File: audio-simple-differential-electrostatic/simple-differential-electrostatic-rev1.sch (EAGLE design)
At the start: 73 parts, among them IC1 LT1115, IC2 LT1115, IC3 LT1115, IC4 LT1115, IC5 LM7815, IC7 LM317T, IC8 LM317T, IC9 LM7915, J1 ROUT, J2 LOUT, J3 VIN_PLATE, X1 RIN, X2 LIN, X3 VIN_OPAMP, X4 VIN_HEATER

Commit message: First gerber export
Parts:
- added C26, C30, C31, C32: 10n, rcl:C-EU050-025X075
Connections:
- net GND: now also C26.2, C30.2, C31.2, C32.2; no longer H1.MOUNT, H2.MOUNT, H3.MOUNT, H4.MOUNT
- net PP_HEATER_N: now also C31.1, C32.1
- net PP_HEATER_P: now also C26.1, C30.1
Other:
- note added: "Heater Decoupling"
- note added: "Net Class: high_voltage"
- moved on the sheet: C1, C2, C3, C4

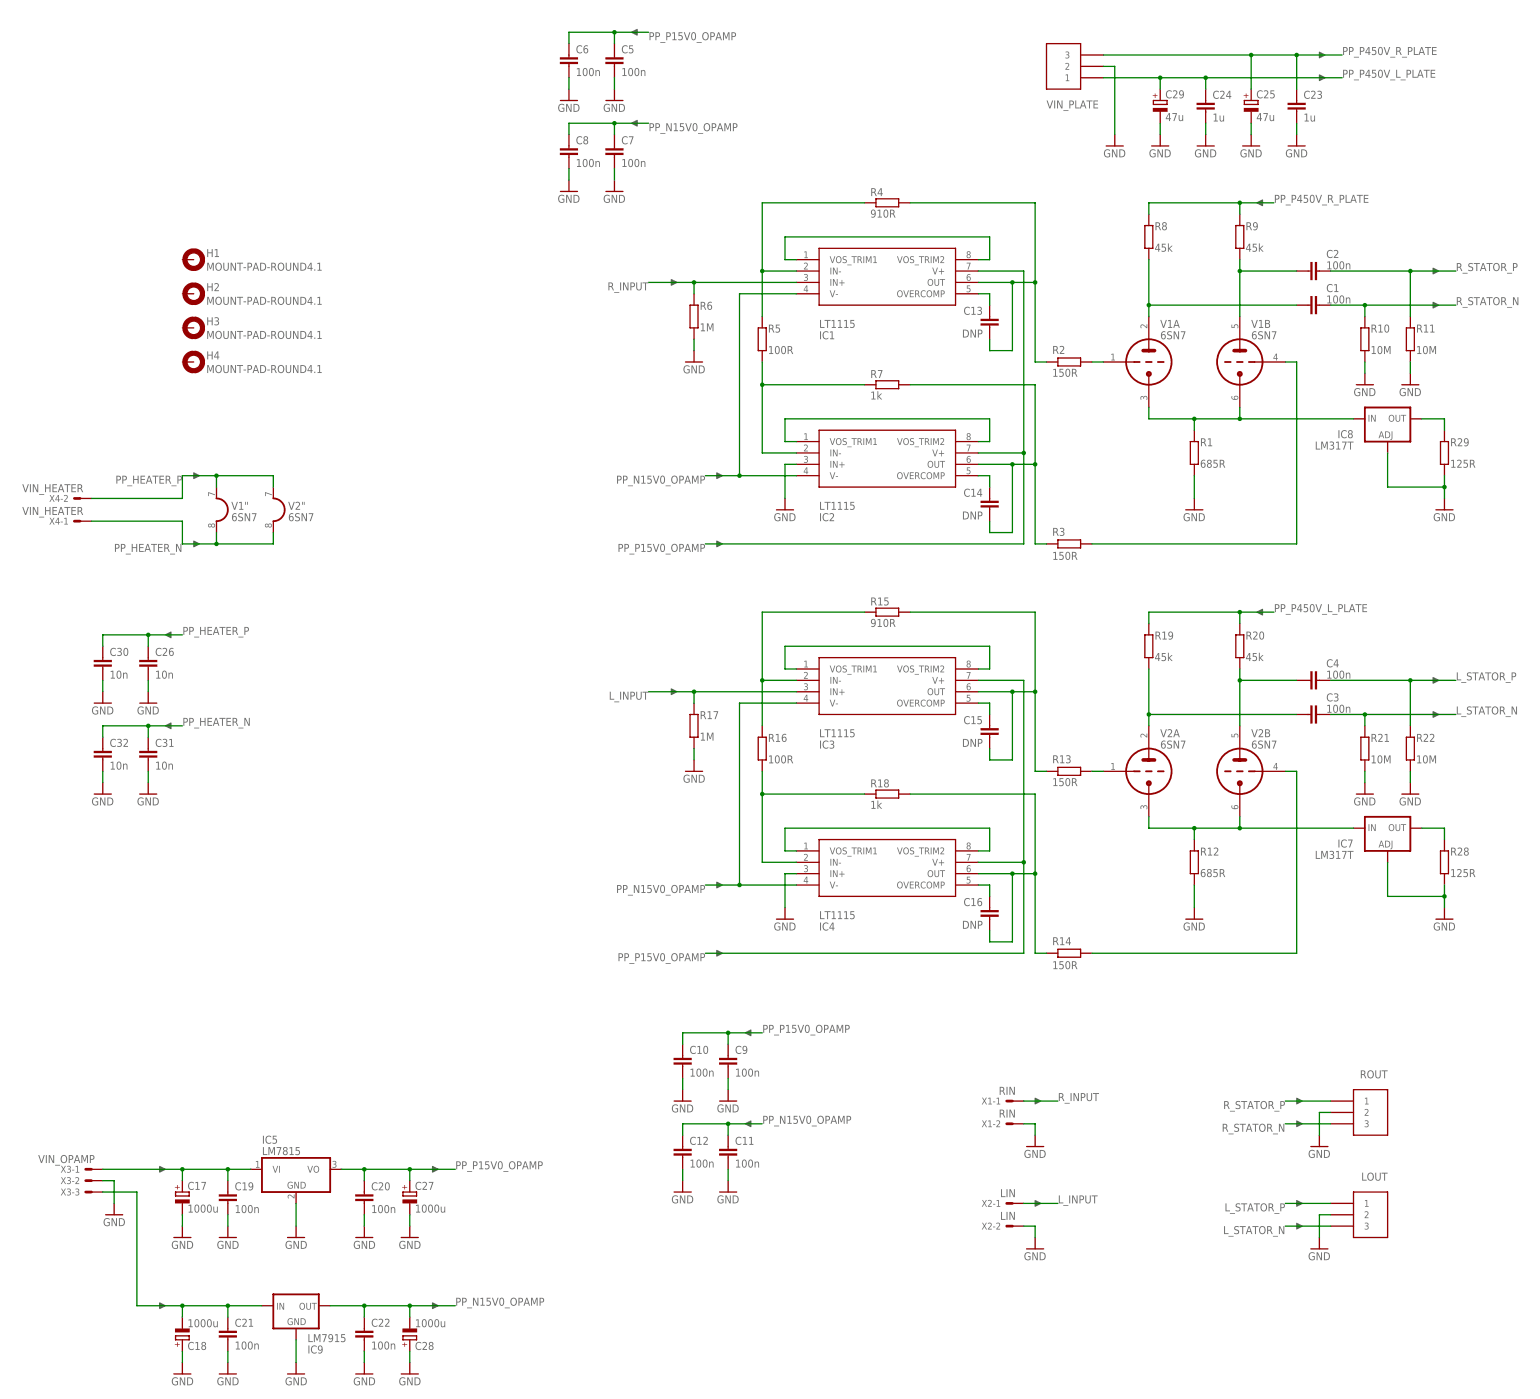
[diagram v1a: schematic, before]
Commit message: Ran cmd-renumber, increased HV clearance to 56mil, re-exported gerbers
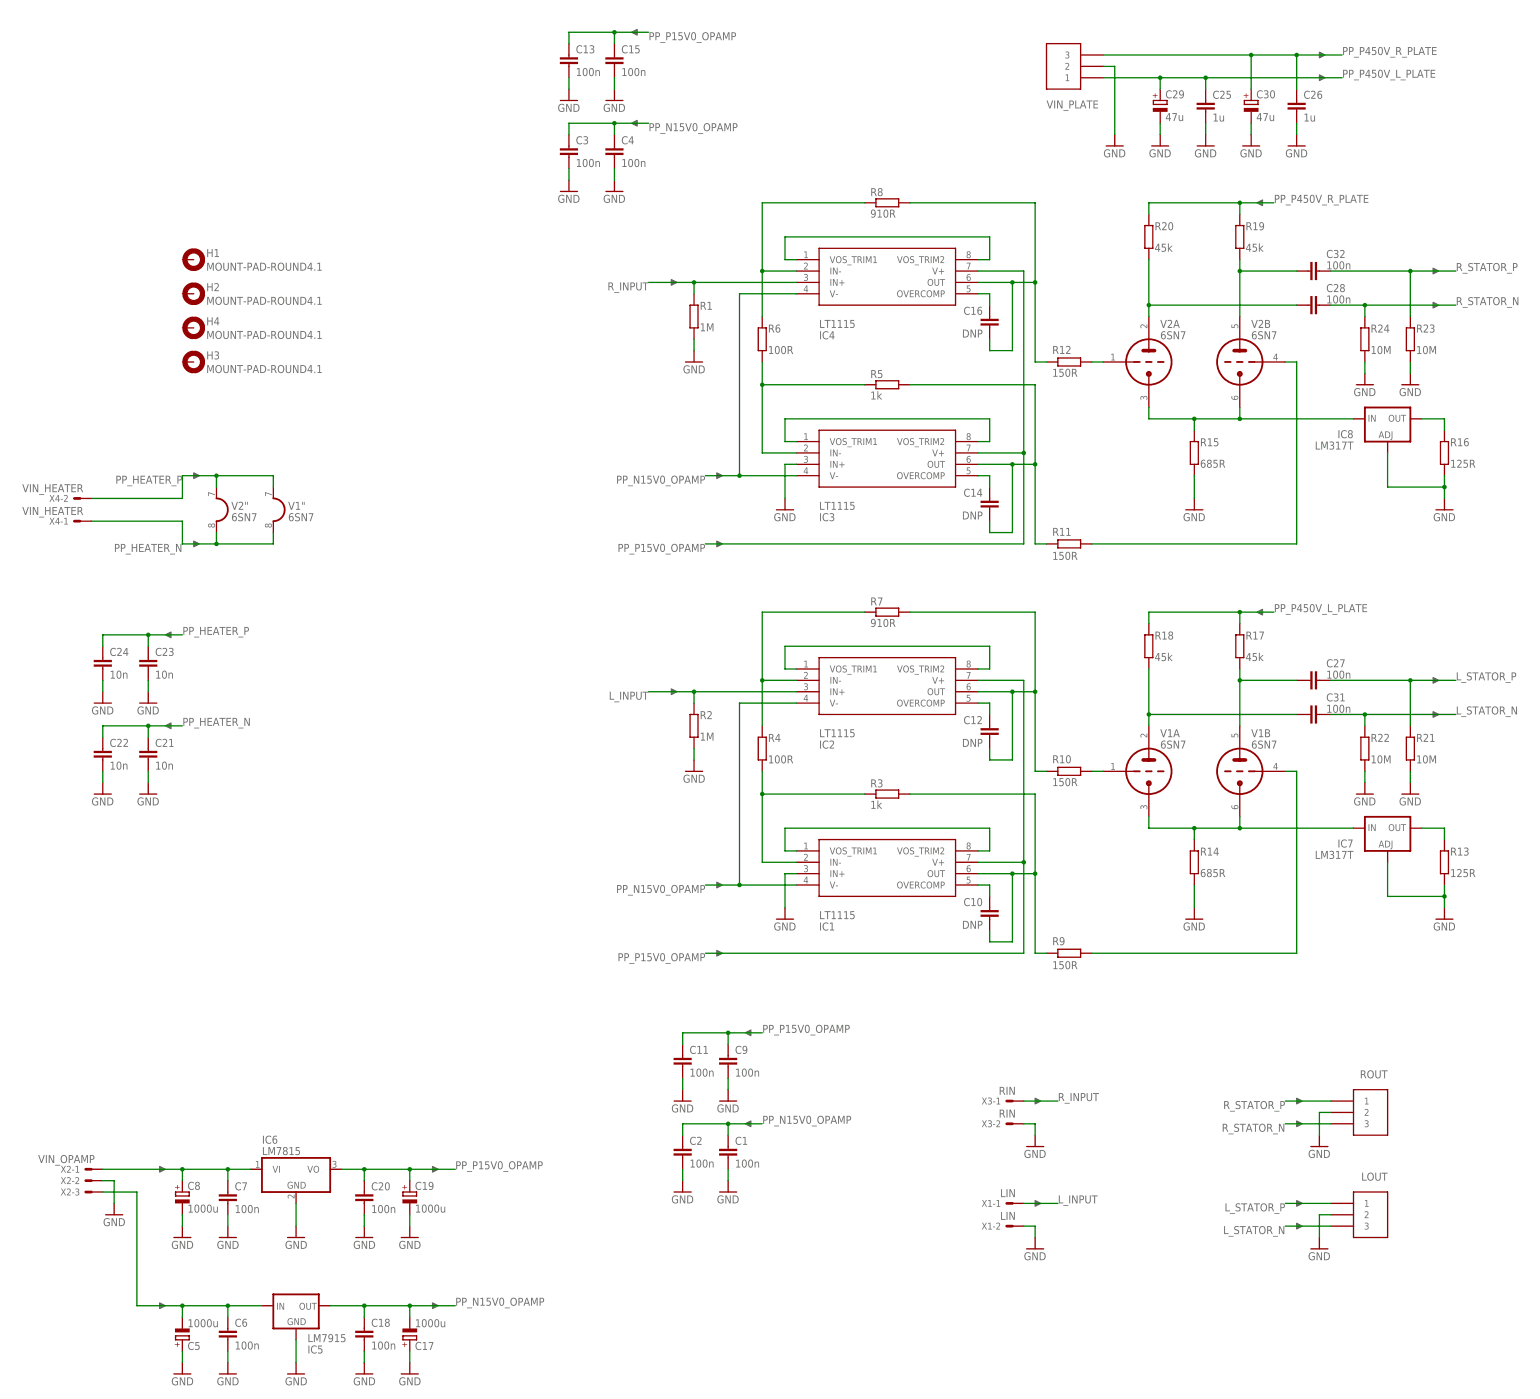
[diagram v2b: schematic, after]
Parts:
- removed IC9: LM7915, v-reg:79XXS
- removed R28, R29: 125R, rcl:R-EU_0309/10
- added IC6: LM7815, linear:7815TV
- added R23, R24: 10M, rcl:R-EU_0309/10
- C1, C2, C3, C4: device rcl:C-EU375-155X418 -> rcl:C-EU050-025X075
- C10, C12: value 100n -> DNP
- C13, C15: value DNP -> 100n
- C18: value 1000u -> 100n; device rcl:CPOL-EUE5-10.5 -> rcl:C-EU050-025X075
- C19, C5, C8: value 100n -> 1000u; device rcl:C-EU050-025X075 -> rcl:CPOL-EUE5-10.5
- C21, C22: value 100n -> 10n
- C23, C24: value 1u -> 10n; device rcl:C-EU325-137X374 -> rcl:C-EU050-025X075
- C25: value 47u -> 1u; device rcl:CPOL-EUE10-22.5 -> rcl:C-EU325-137X374
- C26: value 10n -> 1u; device rcl:C-EU050-025X075 -> rcl:C-EU325-137X374
- C27, C28: value 1000u -> 100n; device rcl:CPOL-EUE5-10.5 -> rcl:C-EU375-155X418
- C30: value 10n -> 47u; device rcl:C-EU050-025X075 -> rcl:CPOL-EUE10-22.5
- C31, C32: value 10n -> 100n; device rcl:C-EU050-025X075 -> rcl:C-EU375-155X418
- IC5: value LM7815 -> LM7915; device linear:7815TV -> v-reg:79XXS
- J1: value ROUT -> LOUT
- J2: value LOUT -> VIN_PLATE; VALUE (none) -> MOLEX_0039302031
- J3: value VIN_PLATE -> ROUT; VALUE MOLEX_0039302031 -> (none)
- R1: value 685R -> 1M
- R10, R11: value 10M -> 150R
- R12: value 685R -> 150R
- R13: value 150R -> 125R
- R14: value 150R -> 685R
- R15: value 910R -> 685R
- R16: value 100R -> 125R
- R17: value 1M -> 45k; device rcl:R-EU_0309/10 -> rcl:R-EU_0613/15
- R18: value 1k -> 45k; device rcl:R-EU_0309/10 -> rcl:R-EU_0613/15
- R2: value 150R -> 1M
- R3: value 150R -> 1k
- R4: value 910R -> 100R
- R5: value 100R -> 1k
- R6: value 1M -> 100R
- R7: value 1k -> 910R
- R8: value 45k -> 910R; device rcl:R-EU_0613/15 -> rcl:R-EU_0309/10
- R9: value 45k -> 150R; device rcl:R-EU_0613/15 -> rcl:R-EU_0309/10
- X1: value RIN -> LIN
- X2: value LIN -> VIN_OPAMP; device con-molex:KK-156-2 -> con-molex:KK-156-3
- X3: value VIN_OPAMP -> RIN; device con-molex:KK-156-3 -> con-molex:KK-156-2
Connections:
- removed net N$26 (its old number): C13.1, IC1.OVERCOMP
- new net N$31: C10.1, IC1.OVERCOMP
- net GND: now also C1.2, C13.2, C15.2, C17.+, C18.2, C19.-, C2.2, C25.2, C3.2, C30.-, C4.2, C5.+, C8.-, IC1.IN+, IC3.IN+, IC6.GND, R13.1, R14.1, R15.1, R16.1, R2.1, R23.1, R24.1; no longer C10.2, C12.2, C17.-, C18.+, C19.2, C25.-, C27.-, C28.+, C30.2, C31.2, C32.2, C5.2, C8.2, IC2.IN+, IC4.IN+, IC9.GND, R10.1, R11.1, R12.1, R17.1, R28.1, R29.1, R6.1
- net L_INPUT: now also IC2.IN+, R2.2, X1-1.S; no longer IC3.IN+, R17.2, X2-1.S
- net L_STATOR_N: now also C31.2, J1.3, R22.2; no longer C3.2, J2.3, R21.2
- net L_STATOR_P: now also C27.2, J1.1, R21.2; no longer C4.2, J2.1, R22.2
- net N$1: now also R15.2, V2A.TK, V2B.TK; no longer R1.2, V1A.TK, V1B.TK
- net N$10: now also IC4.IN-, R6.1, R8.1; no longer IC1.IN-, R4.1, R5.1
- net N$12: now also C27.1, R17.1, V1B.TA; no longer C4.1, R20.1, V2B.TA
- net N$13: now also IC3.IN-, R5.1, R6.2; no longer IC2.IN-, R5.2, R7.1
- net N$14: now also IC3.OUT, R11.2, R5.2; no longer IC2.OUT, R3.2, R7.2
- net N$15: now also R9.1, V1B.TG; no longer R14.1, V2B.TG
- net N$16: now also R10.1, V1A.TG; no longer R13.1, V2A.TG
- net N$17: now also C12.2, IC2.OUT, R10.2, R7.2; no longer C15.2, IC3.OUT, R13.2, R15.2
- net N$19: now also IC2.IN-, R4.1, R7.1; no longer IC3.IN-, R15.1, R16.1
- net N$2: now also C28.1, R20.1, V2A.TA; no longer C1.1, R8.1, V1A.TA
- net N$21: now also IC1.IN-, R3.1, R4.2; no longer IC4.IN-, R16.2, R18.1
- net N$22: now also C10.2, IC1.OUT, R3.2, R9.2; no longer C16.2, IC4.OUT, R14.2, R18.2
- net N$25: now also R16.2; no longer R29.2
- net N$27: now also IC3.OVERCOMP; no longer IC2.OVERCOMP
- net N$28: now also C5.-, C6.1, IC5.IN, X2-3.S; no longer C18.-, C21.1, IC9.IN, X3-3.S
- net N$29: now also C12.1, IC2.OVERCOMP; no longer C15.1, IC3.OVERCOMP
- net N$3: now also C32.1, R19.1, V2B.TA; no longer C2.1, R9.1, V1B.TA
- net N$30: now also C7.1, C8.+, IC6.VI, X2-1.S; no longer C17.+, C19.1, IC5.VI, X3-1.S
- net N$36: now also R13.2; no longer R28.2
- net N$4: now also C16.2, IC4.OUT, R12.2, R8.2; no longer C13.2, IC1.OUT, R2.2, R4.2
- net N$5: now also R14.2, V1A.TK, V1B.TK; no longer R12.2, V2A.TK, V2B.TK
- net N$6: now also C31.1, R18.1, V1A.TA; no longer C3.1, R19.1, V2A.TA
- net N$7: now also R11.1, V2B.TG; no longer R3.1, V1B.TG
- net N$8: now also R12.1, V2A.TG; no longer R2.1, V1A.TG
- net PP_HEATER_N: now also C21.1, C22.1; no longer C31.1, C32.1
- net PP_HEATER_P: now also C23.1, C24.1; no longer C26.1, C30.1
- net PP_N15V0_OPAMP: now also C1.1, C17.-, C18.1, C2.1, C3.1, C4.1, IC5.OUT; no longer C11.1, C12.1, C22.1, C28.-, C7.1, C8.1, IC9.OUT
- net PP_P15V0_OPAMP: now also C11.1, C13.1, C15.1, C19.+, IC6.VO; no longer C10.1, C27.+, C5.1, C6.1, IC5.VO
- net PP_P450V_L_PLATE: now also C25.1, J2.1, R17.2, R18.2; no longer C24.1, J3.1, R19.2, R20.2
- net PP_P450V_R_PLATE: now also C26.1, C30.+, J2.3, R19.2, R20.2; no longer C23.1, C25.+, J3.3, R8.2, R9.2
- net R_INPUT: now also IC4.IN+, R1.2, X3-1.S; no longer IC1.IN+, R6.2, X1-1.S
- net R_STATOR_N: now also C28.2, J3.3, R24.2; no longer C1.2, J1.3, R10.2
- net R_STATOR_P: now also C32.2, J3.1, R23.2; no longer C2.2, J1.1, R11.2
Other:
- note added: "Clearance: Min. 32mil for external coated conductors at 500V"
- moved on the sheet: C1, C10, C11, C12, C13, C15, C16, C17, C2, C21, C22, C23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

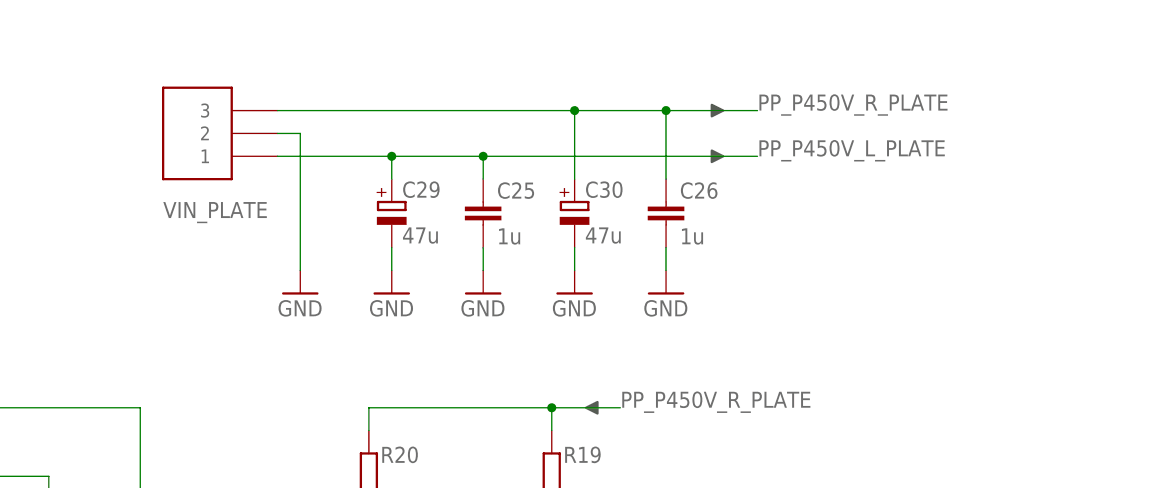
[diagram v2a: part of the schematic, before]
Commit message: Moved to PQC rev. 1.1 --- fixed hysteresis resistor connection.
Hysteresis resistor (R3) should be connected to comparator negative
supply rail, not GND. Re-exported Gerbers.
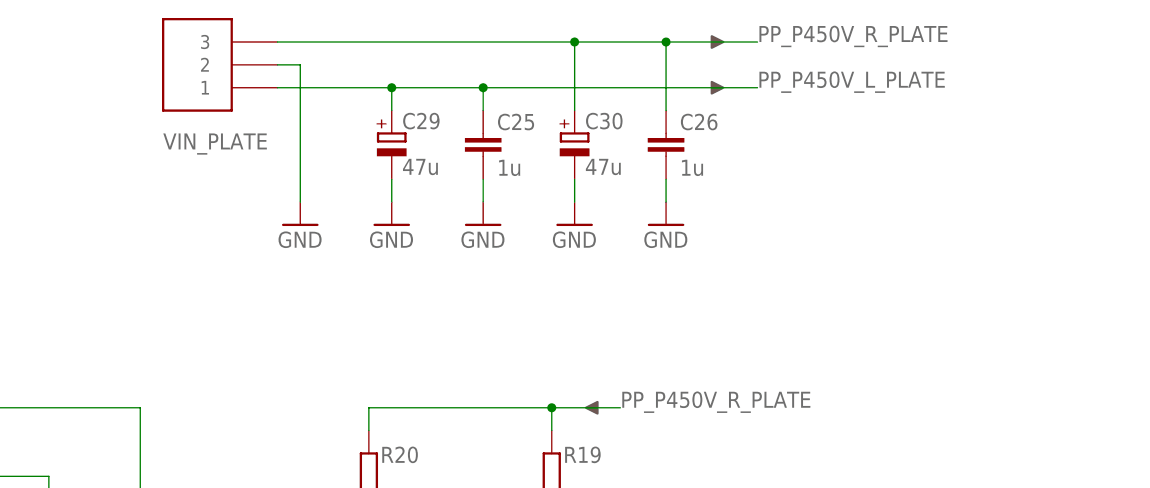
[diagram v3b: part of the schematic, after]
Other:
- note added: "(7.56W total)"
- note added: "Pop. either R14 or IC7"
- note added: "Pop. either R15 or IC8"
- note added: "Total Left-Plate Power = 4.5W"
- note added: "Total Right-Plate Power = 4.5W"
- note removed: "Pop. either R1 or IC8"
- note removed: "Pop. either R12 or IC7"
- moved on the sheet: C25, C26, C29, C30

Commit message: Added opamp output pulldowns, rerouted, switched sch to multiple pages
Opamp pulldowns bias output stage into class A
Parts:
- added R25, R26, R27, R28: 10k, rcl:R-EU_0309/10
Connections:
- net N$14: now also R28.2
- net N$17: now also R25.2
- net N$22: now also R26.2
- net N$4: now also R27.2
- net PP_N15V0_OPAMP: now also R25.1, R26.1, R27.1, R28.1
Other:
- note added: "1"
- note added: "1 of 1"
- note added: "1.0"
- note added: "2"
- note added: "3"
- note added: "4"
- note added: "CONTENTS"
- note added: "Daniel Kramnik"
- note added: "Keep appropriate clearances to high_voltage net class"
- note added: "LEFT CHANNEL"
- note added: "LINEAR ACTIVE SPAD QUENCHING CIRCUIT"
- note added: "POWER SUPPLIES"
- note added: "RIGHT CHANNEL"
- note added: "Routing Notes:"
- note added: "SHEET"
- note added: "TABLE OF CONTENTS"
